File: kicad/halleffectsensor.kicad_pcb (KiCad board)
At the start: 2 copper layers, 80 x 28 mm, 26 parts, among them J1 Conn_01x03, J2 Conn_01x02, Q1 2N3904, U3 ER_OLEDM0.91_1x-I2C, U5 XIAO-nRF52840-SMD

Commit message: Finished PCB and BOM
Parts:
- U2: footprint Package_SO:SOIC-8_4.4x5.0mm_P1.27mm -> Package_SO:JEITA_SOIC-8_3.9x4.9mm_P1.27mm
- turned U2 to 180 degrees
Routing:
- net Net-(R11-Pad2): track 29.5 -> 28.4 mm

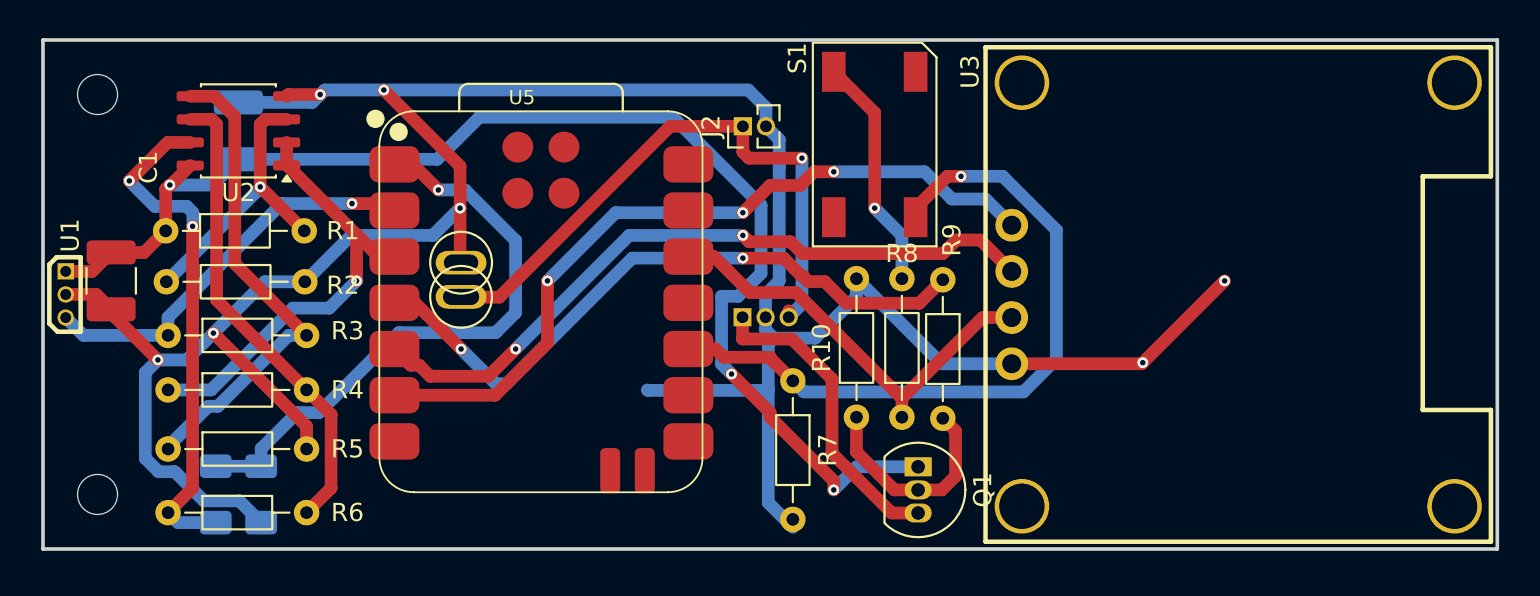
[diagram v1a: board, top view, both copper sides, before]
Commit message: Update pcb because github didn't work for some reason
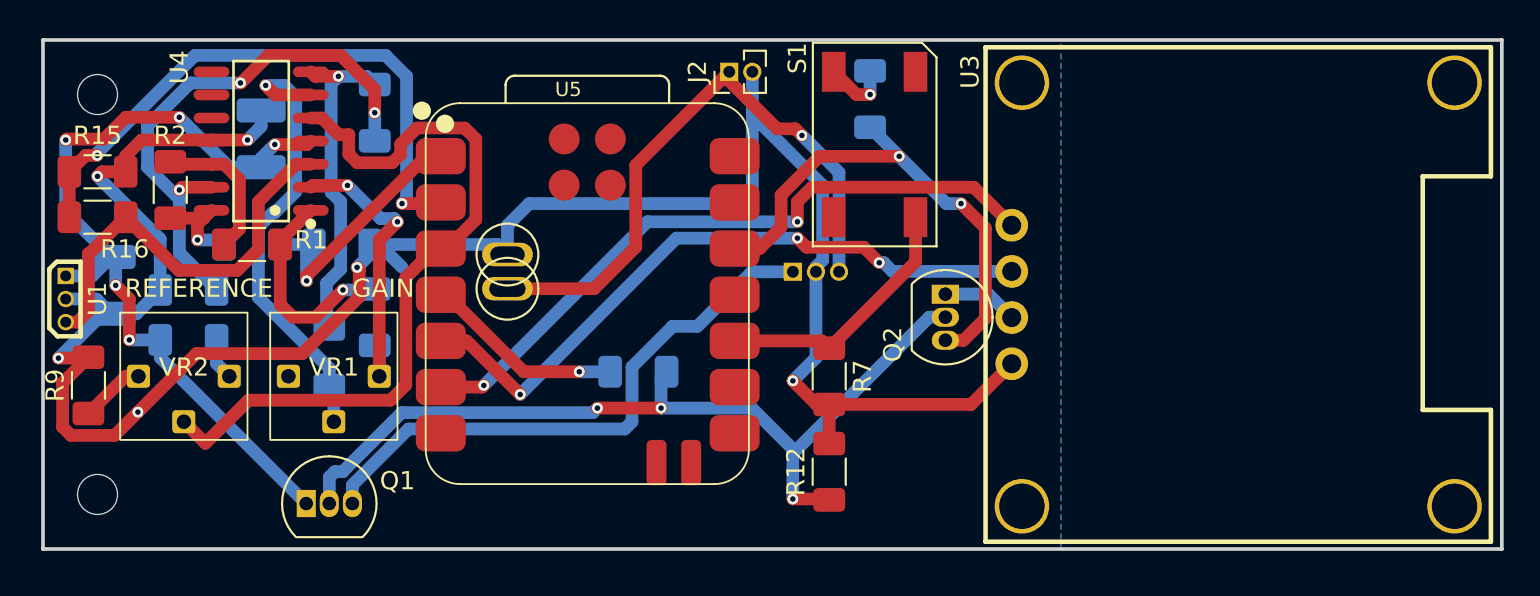
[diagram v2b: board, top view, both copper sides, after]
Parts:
- removed U2: ~, Package_SO:JEITA_SOIC-8_3.9x4.9mm_P1.27mm
- added Q2: 2N3904, Package_TO_SOT_THT:TO-92_Inline, F.Cu at (149.6, 114.0)
- added R15: 470R, Resistor_SMD:R_1206_3216Metric_Pad1.30x1.75mm_HandSolder, F.Cu at (103.0, 109.8)
- added R16: 910R, Resistor_SMD:R_1206_3216Metric_Pad1.30x1.75mm_HandSolder, F.Cu at (103.0, 107.2)
- added R17: 470R, Resistor_SMD:R_1206_3216Metric_Pad1.30x1.75mm_HandSolder, B.Cu at (111.5, 111.2)
- added R18: 910R, Resistor_SMD:R_1206_3216Metric_Pad1.30x1.75mm_HandSolder, B.Cu at (116.5, 111.2)
- added U4: ~, easyeda2kicad:SOP-14_L8.6-W3.9-P1.27-LS6.0-BL, F.Cu at (112.0, 105.6)
- added VR1: ~, easyeda2kicad:Potentiometer_3_pi, F.Cu at (116.0, 118.5)
- added VR2: ~, easyeda2kicad:Potentiometer_3_pi, F.Cu at (107.8, 118.5)
- C1: moved to B.Cu
- R1, R2: value R -> 10k; footprint Resistor_THT:R_Axial_DIN0204_L3.6mm_D1.6mm_P7.62mm_Horizontal -> Resistor_SMD:R_1206_3216Metric_Pad1.30x1.75mm_HandSolder
- R10: value 470kR -> 10k; footprint Resistor_THT:R_Axial_DIN0204_L3.6mm_D1.6mm_P7.62mm_Horizontal -> Resistor_SMD:R_1206_3216Metric_Pad1.30x1.75mm_HandSolder; moved to B.Cu
- R12: value 910R -> 10kR; moved to F.Cu
- R3, R4, R5, R6: value R -> 10k; footprint Resistor_THT:R_Axial_DIN0204_L3.6mm_D1.6mm_P7.62mm_Horizontal -> Resistor_SMD:R_1206_3216Metric_Pad1.30x1.75mm_HandSolder; moved to B.Cu
- R7: value 470kR -> 10kR; footprint Resistor_THT:R_Axial_DIN0204_L3.6mm_D1.6mm_P7.62mm_Horizontal -> Resistor_SMD:R_1206_3216Metric_Pad1.30x1.75mm_HandSolder
- R8: value 4.7k -> 470R; footprint Resistor_THT:R_Axial_DIN0204_L3.6mm_D1.6mm_P7.62mm_Horizontal -> Resistor_SMD:R_1206_3216Metric_Pad1.30x1.75mm_HandSolder; moved to B.Cu
- R9: value 4.7k -> 10k; footprint Resistor_THT:R_Axial_DIN0204_L3.6mm_D1.6mm_P7.62mm_Horizontal -> Resistor_SMD:R_1206_3216Metric_Pad1.30x1.75mm_HandSolder
- moved R9 47.4 mm to (102.5, 119.0), turned to 90 degrees
- moved R10 37.0 mm to (108.0, 116.5), turned to 0 degrees
- moved Q1 33.7 mm to (114.5, 125.5), turned to 0 degrees
- moved R12 31.3 mm to (143.2, 123.8)
- moved R11 24.2 mm to (132.8, 118.2), turned to 180 degrees
- moved R8 17.6 mm to (145.5, 103.2)
- moved R3 16.7 mm to (118.2, 104.0), turned to -90 degrees
- moved R5 13.5 mm to (118.2, 115.2), turned to -90 degrees
- moved R6 12.3 mm to (115.8, 117.5), turned to 90 degrees
- moved R4 5.61 mm to (108.0, 113.8), turned to 180 degrees
- moved R2 5.05 mm to (107.0, 108.2), turned to 90 degrees
- moved R1 4.81 mm to (111.5, 111.2), turned to 180 degrees
- moved J1 3.73 mm to (141.2, 112.8)
- moved J2 3.09 mm to (137.8, 101.8)
- moved REF** 2.59 mm to (125.5, 111.8)
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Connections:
- net /WAKEUP renamed /BTN
- Q1 pad 2: Net-(Q1-B) -> /CTRL_PWR
- R1 pad 1: 5V -> Net-(R1-Pad1)
- R1 pad 2: Net-(U2A-+) -> Net-(U4C-+)
- R10 pad 1: Net-(Q1-B) -> 5V
- R10 pad 2: GND -> Net-(R10-Pad2)
- R11 pad 1: /OUT -> /CTRL_PWR
- R11 pad 2: Net-(R11-Pad2) -> Net-(U5-D3)
- R12 pad 1: GND -> /CTRL_PWR
- R12 pad 2: /OUT -> GND
- R2 pad 1: Net-(U2A-+) -> Net-(R17-Pad2)
- R2 pad 2: GND -> Net-(U4C-+)
- R3 pad 1: /RAW_OUT -> Net-(R3-Pad1)
- R3 pad 2: Net-(U2B-+) -> Net-(U4C--)
- R4 pad 1: /REF_SIG -> Net-(U4C--)
- R4 pad 2: Net-(U2B--) -> GND
- R5 pad 1: Net-(U2B-+) -> Net-(R1-Pad1)
- R5 pad 2: GND -> Net-(U4A--)
- R6 pad 1: Net-(R11-Pad2) -> Net-(U4B--)
- R6 pad 2: Net-(U2B--) -> Net-(R3-Pad1)
- R9 pad 1: /CTRL_5V -> Net-(R9-Pad1)
- R9 pad 2: Net-(Q1-B) -> GND
- U3 pad 2: 3V3 -> Net-(Q2-E)
- U5 pad 1: /OUT -> /OUT_3V3
- U5 pad 2: /RAW_OUT -> /RAW_OUT_3V3
- U5 pad 3: /REF_SIG -> /REF_SIG_SCALED
- U5 pad 4: /CTRL_5V -> Net-(U5-D3)
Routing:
- net /CTRL_PWR: track 0.00 -> 47.8 mm, vias 0 -> 3
- net /REF_SIG_SCALED: track 0.00 -> 43.2 mm
- net /CTRL_5V: track 36.4 -> 0.00 mm, vias 2 -> 0
- net /RAW_OUT_3V3: track 0.00 -> 33.8 mm, vias 0 -> 2
- net /OUT: track 32.9 -> 0.00 mm, vias 1 -> 0
- net Net-(U4C--): track 0.00 -> 30.6 mm, vias 0 -> 3
- net GND: track 153.5 -> 123.4 mm, vias 7 -> 6
- net Net-(R11-Pad2): track 28.4 -> 0.00 mm, vias 2 -> 0
- net Net-(U2B-+): track 26.9 -> 0.00 mm
- net Net-(U2B--): track 26.1 -> 0.00 mm
- net 5V: track 71.5 -> 45.4 mm, vias 3 -> 5
- net Net-(U4B--): track 0.00 -> 25.1 mm, vias 0 -> 1
- net /BTN: track 39.3 -> 14.5 mm, vias 1 -> 0
- net /REF_SIG: track 24.7 -> 0.00 mm, vias 1 -> 0
- net Net-(R3-Pad1): track 0.00 -> 18.5 mm, vias 0 -> 1
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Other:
- board size 80 x 28 mm -> 80.2 x 28 mm
- board text added: "5V GND VBAT"
- board text added: "GAIN"
- board text added: "REFERENCE"

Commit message: Worked on the code and fixed an issue with pcb
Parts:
- added R13: 470R, Resistor_SMD:R_1206_3216Metric_Pad1.30x1.75mm_HandSolder, F.Cu at (148.0, 122.4)
- added R14: 10kR, Resistor_SMD:R_1206_3216Metric_Pad1.30x1.75mm_HandSolder, F.Cu at (148.0, 125.7)
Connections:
- Q2 pad 2: /CTRL_PWR -> /CTRL_OLED
- U5 pad 11: unconnected-(U5-D10-Pad11) -> Net-(U5-D10)
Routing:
- net Net-(U5-D10): track 0.00 -> 14.2 mm, vias 0 -> 2
- net /CTRL_OLED: track 0.00 -> 13.2 mm, vias 0 -> 1
- net /CTRL_PWR: track 47.8 -> 36.3 mm
- net GND: track 123.4 -> 128.2 mm

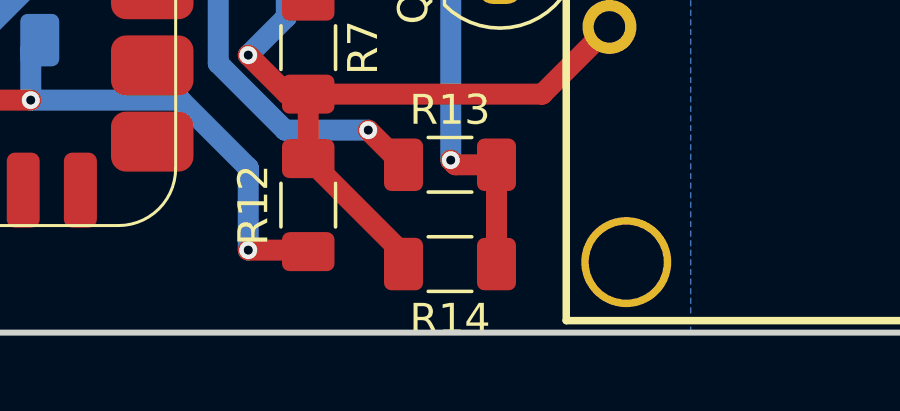
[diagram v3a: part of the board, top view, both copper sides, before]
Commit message: Fix BOM and update pcb
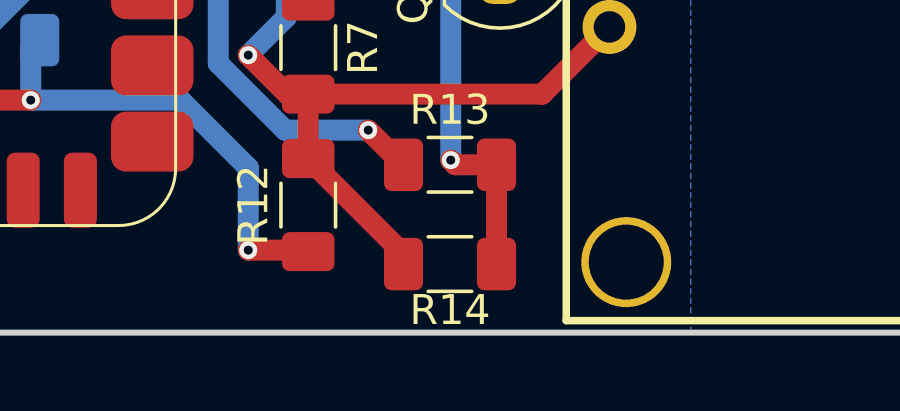
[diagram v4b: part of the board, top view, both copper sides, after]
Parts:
- R11, R13: value 470R -> 910R
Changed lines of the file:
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@@
 		(tags "resistor handsolder")
 		(property "Reference" "R14"
-			(at 0 -1.83 0)
+			(at 0 -1.535 0)
 			(layer "F.SilkS")
 			(effects
@@
 			)
 		)
-		(property "Value" "470R"
+		(property "Value" "910R"
 			(at 0 1.83 0)
 			(layer "F.Fab")
@@
 			)
 		)
-		(property "Value" "470R"
+		(property "Value" "910R"
 			(at 0 -1.83 0)
 			(layer "B.Fab")

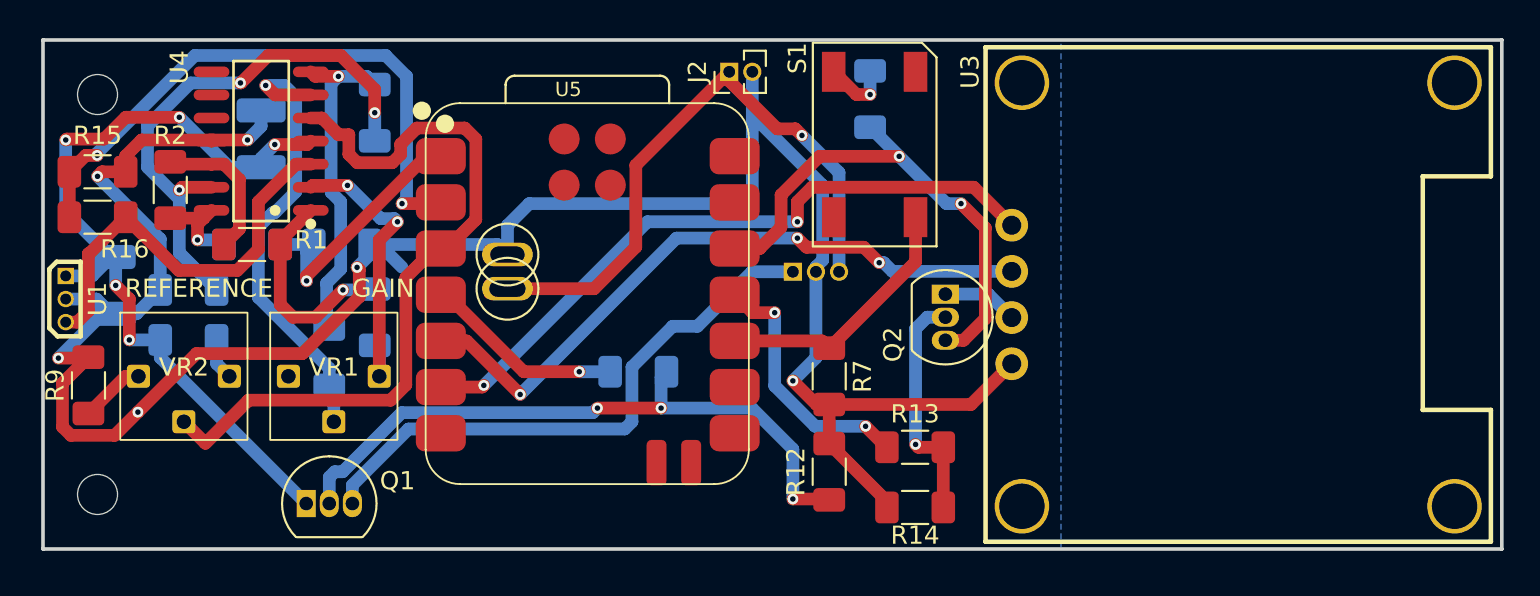
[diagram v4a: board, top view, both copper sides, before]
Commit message: Remove plated through holes and remove item from BOM no longer needed
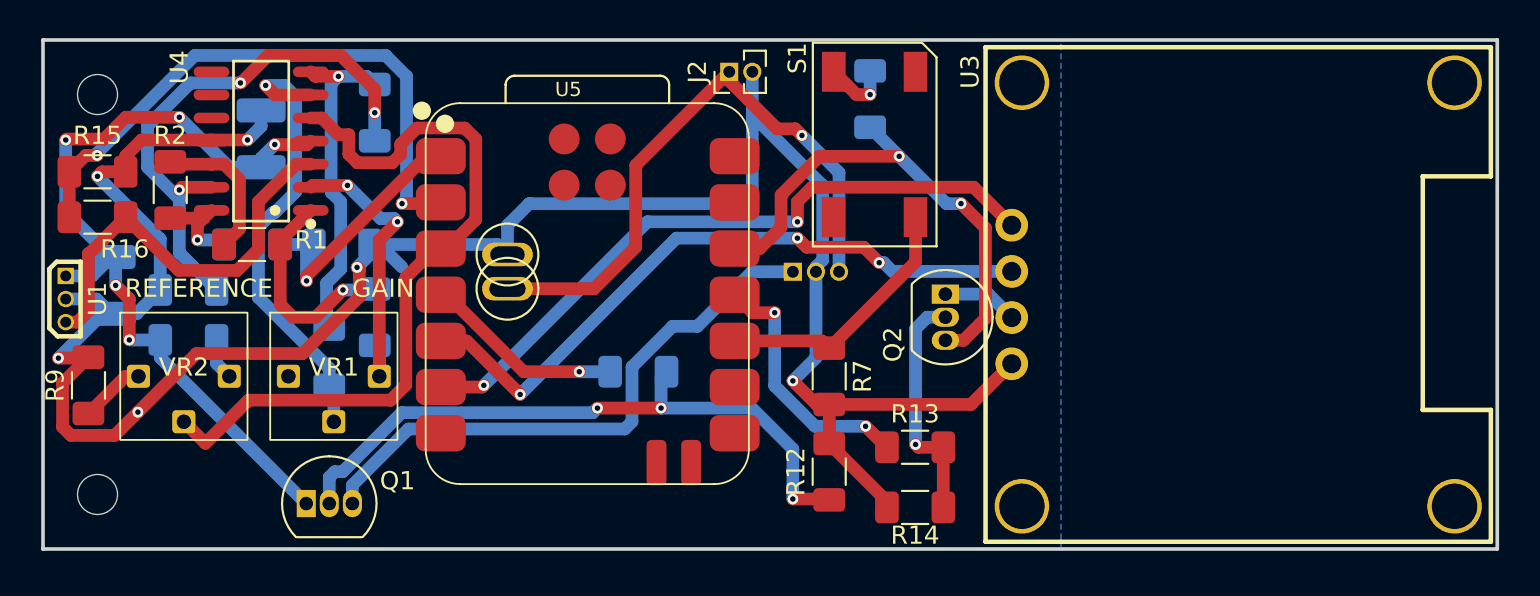
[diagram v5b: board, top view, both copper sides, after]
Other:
- board size 80.2 x 28 mm -> 80 x 28 mm
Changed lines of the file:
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@@
 			)
 		)
-		(pad "" thru_hole circle
+		(pad "" np_thru_hole circle
 			(at -11.65 0.56 90)
 			(size 3 3)
 			(drill 2.5)
 			(layers "*.Cu" "*.Mask")
-			(remove_unused_layers no)
-		)
-		(pad "" thru_hole circle
+		)
+		(pad "" np_thru_hole circle
 			(at -11.65 24.36 90)
 			(size 3 3)
 			(drill 2.5)
 			(layers "*.Cu" "*.Mask")
-			(remove_unused_layers no)
-		)
-		(pad "" thru_hole circle
+		)
+		(pad "" np_thru_hole circle
 			(at 11.65 0.56 90)
 			(size 3 3)
 			(drill 2.5)
 			(layers "*.Cu" "*.Mask")
-			(remove_unused_layers no)
-		)
-		(pad "" thru_hole circle
+		)
+		(pad "" np_thru_hole circle
 			(at 11.65 24.36 90)
 			(size 3 3)
 			(drill 2.5)
 			(layers "*.Cu" "*.Mask")
-			(remove_unused_layers no)
 		)
 		(pad "1" thru_hole circle
@@
 	(gr_rect
 		(start 100 100)
-		(end 180.25 128)
+		(end 180 128)
 		(stroke
 			(width 0.2)

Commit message: Fixed the high side mosfets
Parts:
- added C3: C, Capacitor_SMD:C_1210_3225Metric_Pad1.33x2.70mm_HandSolder, B.Cu at (112.0, 121.5)
- added C4: C, Capacitor_THT:C_Radial_D4.0mm_H7.0mm_P1.50mm, F.Cu at (107.2, 125.2)
- added Q3: AO3400A, Package_TO_SOT_SMD:SOT-23, F.Cu at (114.3, 125.2)
- added Q4: AO3401A, Package_TO_SOT_SMD:SOT-23, F.Cu at (118.8, 125.0)
- added R19: 10k, Resistor_SMD:R_1206_3216Metric_Pad1.30x1.75mm_HandSolder, F.Cu at (149.2, 115.8)
- added R20: 10k, Resistor_SMD:R_1206_3216Metric_Pad1.30x1.75mm_HandSolder, B.Cu at (117.2, 125.0)
- Q1: value 2N3904 -> AO3400A; footprint Package_TO_SOT_THT:TO-92_Inline -> Package_TO_SOT_SMD:SOT-23; moved to B.Cu
- Q2: value 2N3904 -> AO3401A; footprint Package_TO_SOT_THT:TO-92_Inline -> Package_TO_SOT_SMD:SOT-23; moved to B.Cu
- moved Q1 33.0 mm to (146.5, 117.5)
- moved Q2 1.03 mm to (149.8, 115.0), turned to 0 degrees
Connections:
- Q1 pad 1: 5V -> /CTRL_OLED
- Q1 pad 2: /CTRL_PWR -> GND
- Q1 pad 3: Net-(J1-Pin_1) -> Net-(Q1-D)
- Q2 pad 1: Net-(Q2-E) -> Net-(Q1-D)
- Q2 pad 2: /CTRL_OLED -> 3V3
- Q2 pad 3: 3V3 -> Net-(Q2-D)
- U3 pad 2: Net-(Q2-E) -> Net-(Q2-D)
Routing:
- net GND: track 128.2 -> 150.2 mm, vias 6 -> 7
- net 5V: track 45.4 -> 57.4 mm
- net Net-(Q3-D): track 0.00 -> 6.39 mm, vias 0 -> 1
- net Net-(Q1-D): track 0.00 -> 6.10 mm, vias 0 -> 1
- net Net-(Q2-E): track 4.18 -> 0.00 mm
- net /CTRL_OLED: track 13.2 -> 9.71 mm
- net Net-(Q2-D): track 0.00 -> 2.65 mm
- net Net-(J1-Pin_1): track 31.9 -> 34.0 mm
- net /CTRL_PWR: track 36.3 -> 37.4 mm, vias 3 -> 4
- net /REF_SIG_SCALED: track 43.2 -> 42.3 mm
- net 3V3: track 28.5 -> 27.8 mm, vias 2 -> 3
